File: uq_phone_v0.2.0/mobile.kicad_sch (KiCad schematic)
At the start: 31 parts, among them J3 20279-001E-03, J4 20279-001E-03, Q1 MMBT3904LP-7, Q2 MMBT3904LP-7, U4 WP SNAP-IN BASE_6000636

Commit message: Clean repo
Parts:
- removed R14, R15, R16: 0R, Resistor_SMD:R_0603_1608Metric, symbol Resistors:Resistor_0R
- R12: renamed from R19; footprint Resistor_SMD:R_0603_1608Metric -> Resistor_SMD:R_0402_1005Metric
- R13: renamed from R20; footprint Resistor_SMD:R_0603_1608Metric -> Resistor_SMD:R_0402_1005Metric
- R14: renamed from R21; footprint Resistor_SMD:R_0603_1608Metric -> Resistor_SMD:R_0402_1005Metric
- R15: renamed from R22; footprint Resistor_SMD:R_0603_1608Metric -> Resistor_SMD:R_0402_1005Metric
- renumbered J3 to J4, J4 to J5, R12 to R16, R13 to R18, R18 to R19, TP9 to TP8, TP8 to TP9
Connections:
- net +VMOB renamed VBAT
- net MOB_USB_N: no longer names the net of U4.12 (USB_D-)
- net MOB_USB_P: no longer names the net of U4.13 (USB_D+)
- no-connect marks 39 -> 42

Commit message: Add more footprints, reduce sizes
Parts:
- C10: footprint Capacitor_SMD:C_0402_1005Metric -> Capacitor_SMD:C_0201_0603Metric; LCSC PN C307331 -> C160831
- C11: footprint Capacitor_SMD:C_0402_1005Metric -> Capacitor_SMD:C_0201_0603Metric; LCSC PN C52923 -> C53067
- R12, R13, R14, R15: LCSC PN C95177 -> (none)
- R16, R17: footprint Resistor_SMD:R_0402_1005Metric -> Resistor_SMD:R_0201_0603Metric; LCSC PN C606173 -> C138135
- R18, R19: footprint Resistor_SMD:R_0402_1005Metric -> Resistor_SMD:R_0201_0603Metric; LCSC PN C427250 -> C138139
- TP10, TP11, TP12, TP13, TP14, TP15, TP16, TP8, TP9: footprint TestPoint:TestPoint_Pad_D1.0mm -> TestPoint:TestPoint_Pad_D1.5mm

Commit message: Various Changes to footprints and components
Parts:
- U4: footprint WP_SNAP-IN_BASE:SIERRA_WP_SNAP-IN_BASE -> RC7620_1104625:XCVR_RC7620_1104625
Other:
- note added: "41"
- title: Power System -> UQ Phone

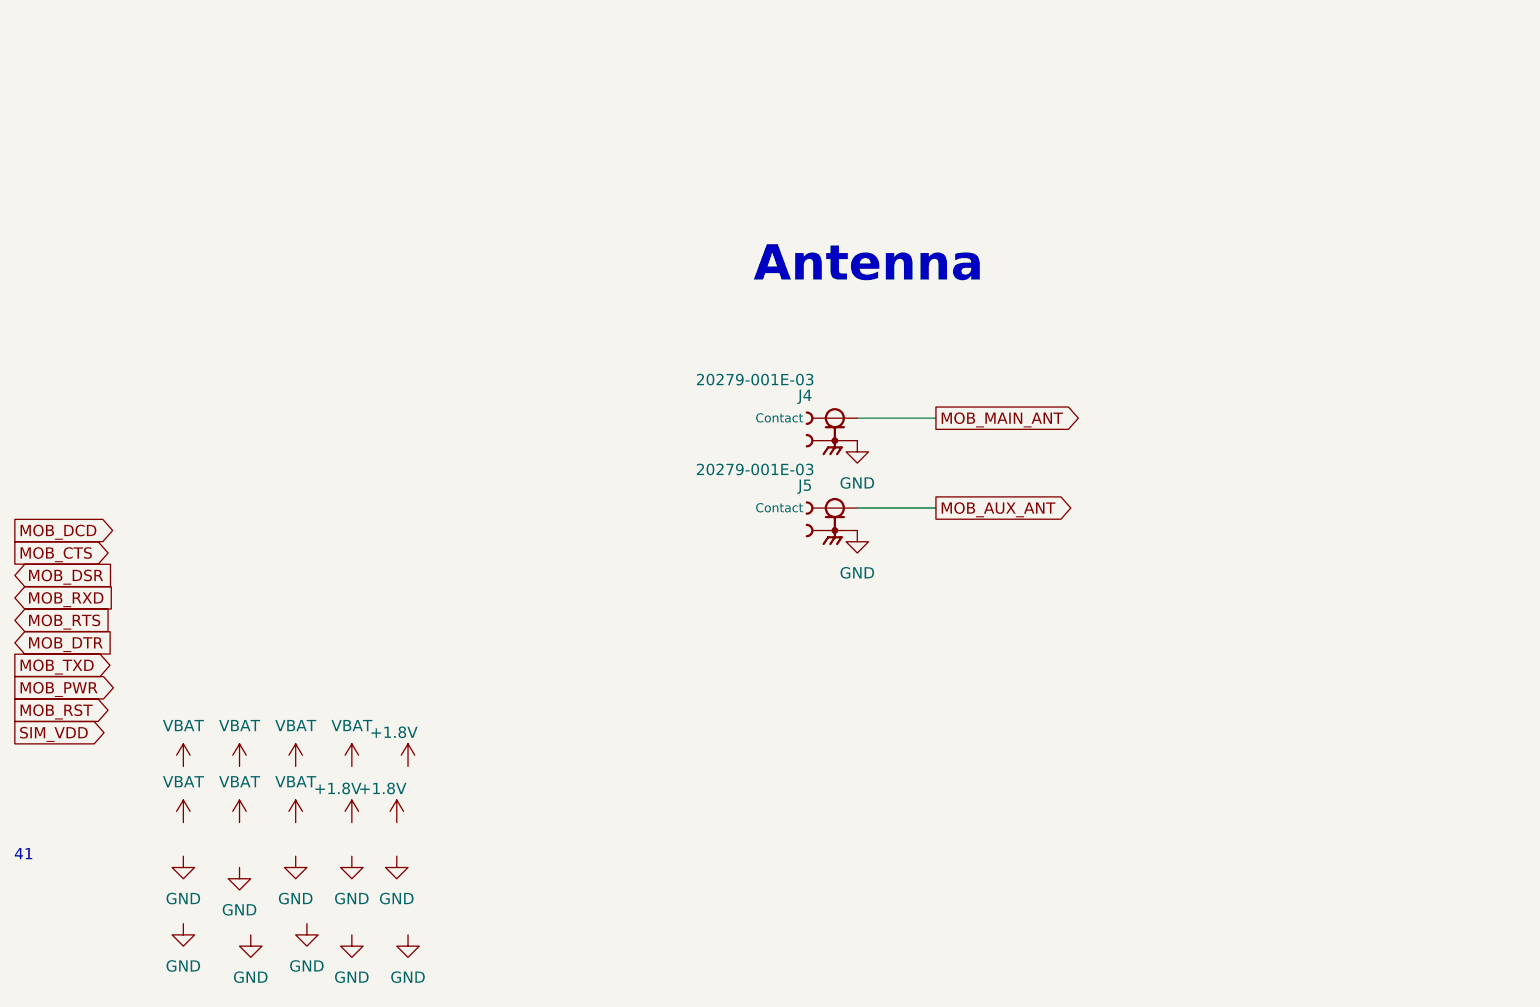
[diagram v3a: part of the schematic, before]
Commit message: Minor Changes - new display
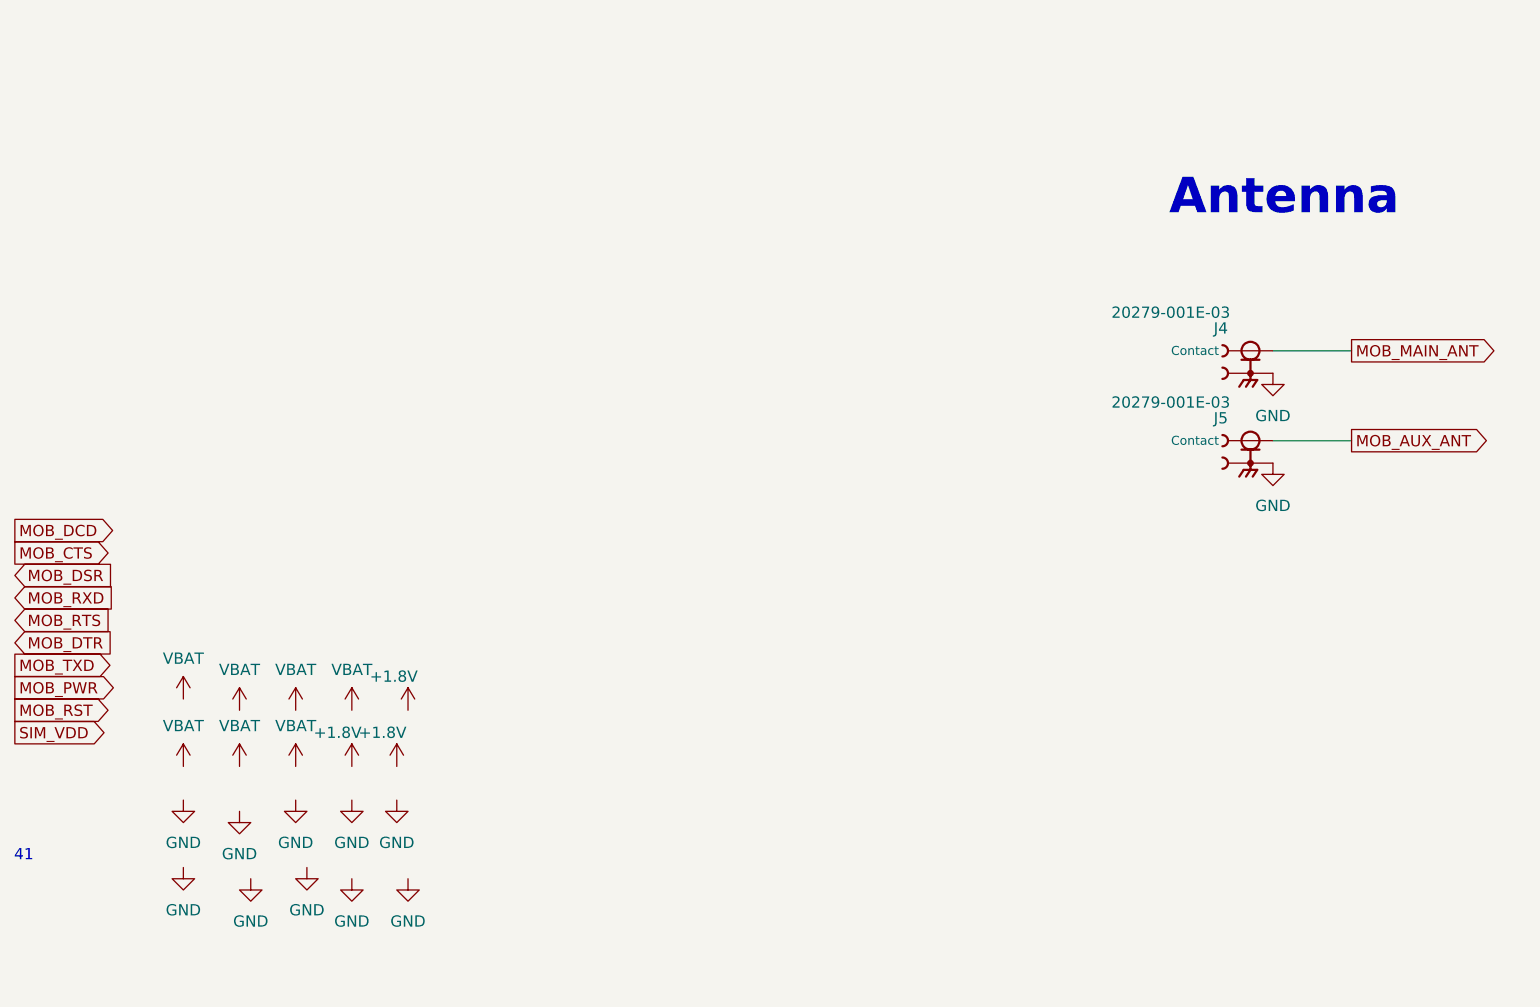
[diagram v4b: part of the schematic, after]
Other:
- moved on the sheet: J4, J5

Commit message: New Layout
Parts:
- removed Q1, Q2: MMBT3904LP-7, MMBT3904LP-7:DFN101X61X53-3N, symbol MMBT3904LP-7:MMBT3904LP-7
- removed R16, R17: 4.7k, Resistor_SMD:R_0201_0603Metric, symbol Resistors:Resistor_4k7
- removed R18, R19: 47k, Resistor_SMD:R_0201_0603Metric, symbol Resistors:Resistor_47k
- added J10, J11: 513382474, 513382474:CON_513382474, symbol 513382474:513382474
- added TP17: TestPoint, TestPoint:TestPoint_Pad_D1.5mm, symbol Connector:TestPoint
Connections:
- net +1.8V: now also J11.10, J11.11, J11.12, J11.9
- net GND: now also J10.23, J10.24, J10.P1, J10.P2, J10.P3, J10.P4, J11.13, J11.14, J11.15, J11.16, J11.17, J11.18, J11.19, J11.20, J11.21, J11.22, J11.23, J11.24, J11.P1, J11.P2, J11.P3, J11.P4
- net SIM_CLK: now also U4.27 (UIM1_CLK); no longer U4.28 (UIM1_DATA)
- net SIM_DATA: now also U4.28 (UIM1_DATA); no longer U4.27 (UIM1_CLK)
- net VBAT: now also J11.1, J11.2, J11.3, J11.4, J11.5, J11.6, J11.7, J11.8, TP17.1
- net MOB_SAFE_PWR_REMOVE: now reaches U4.152 (SAFE_PWR_REMOVE)
- no-connect marks 42 -> 41
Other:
- note added: "0.3A/contact"
- note removed: "41"

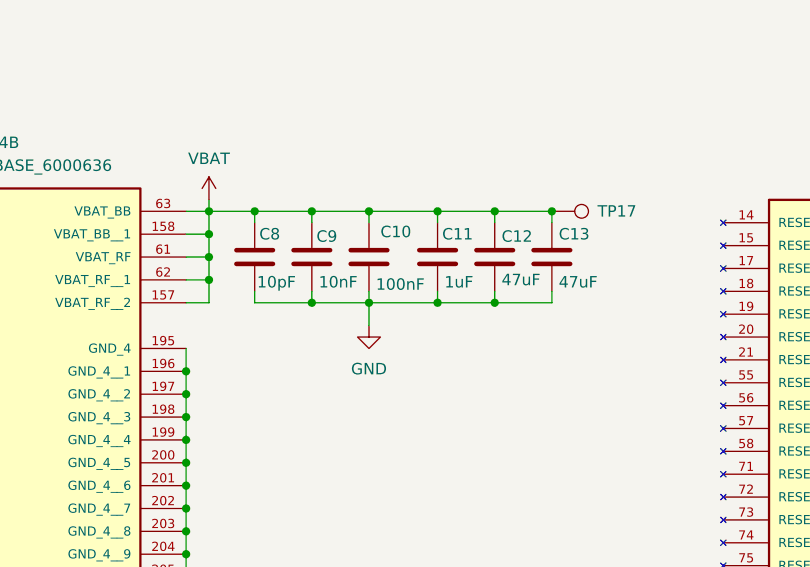
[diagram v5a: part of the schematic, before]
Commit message: Update layout and BL control
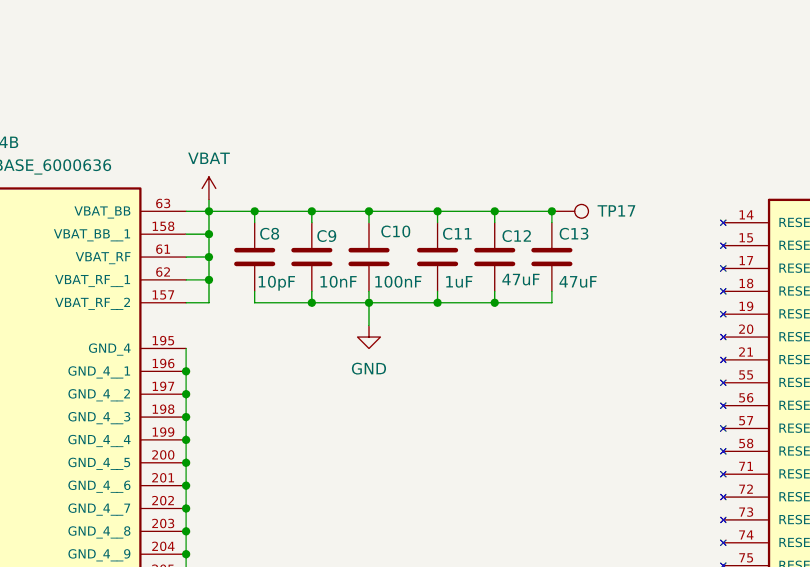
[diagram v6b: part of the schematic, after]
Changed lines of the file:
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@@
 		)
 		(property "Value" "100nF"
-			(at 271.272 46.228 0)
+			(at 271.018 45.974 0)
 			(effects
 				(font

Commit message: Several Hours of Routing
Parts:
- U4: footprint RC7620_1104625:XCVR_RC7620_1104625 -> WP_SNAP-IN_BASE:SIERRA_WP_SNAP-IN_BASE
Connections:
- net +1.8V: now also J11.20, J11.21, J11.22, J11.23; no longer J11.10, J11.11, J11.12, J11.9
- net GND: now also J11.1, J11.10, J11.11, J11.12, J11.2, J11.3, J11.4, J11.5, J11.6, J11.7, J11.8, J11.9; no longer J11.13, J11.14, J11.15, J11.16, J11.17, J11.18, J11.19, J11.20, J11.21, J11.22, J11.23, U4.P1, U4.P10, U4.P11, U4.P12, U4.P13, U4.P14, U4.P15, U4.P16, U4.P17, U4.P18, U4.P19, U4.P2, U4.P20, U4.P3, U4.P4, U4.P5, U4.P6, U4.P7, U4.P8, U4.P9
- net VBAT: now also J11.13, J11.14, J11.15, J11.16, J11.17, J11.18, J11.19; no longer J11.1, J11.2, J11.3, J11.4, J11.5, J11.6, J11.7, J11.8
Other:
- note added: "ADD MORE CAPS"

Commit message: More routing and placements
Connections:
- net MOB_SAFE_PWR_REMOVE is gone; now on net MOB_SAFE_PWR_REMOVE_L: U4.152 (SAFE_PWR_REMOVE)
- net GND: no longer J10.23, J10.24
- net MOB_AUD_BCLK: now also J10.9
- net MOB_AUD_IN: now also J10.10
- net MOB_AUD_OUT: now also J10.11
- net MOB_AUD_SYNC: now also J10.12
- net MOB_CTS: now also J10.18
- net MOB_DCD: now also J10.13
- net MOB_DSR: now also J10.15
- net MOB_DTR: now also J10.14
- net MOB_PWR: now also J10.1
- net MOB_RI: now also J10.20
- net MOB_RST: now also J10.2
- net MOB_RTS: now also J10.17
- net MOB_RXD: now also J10.19
- net MOB_TXD: now also J10.16
- net MOB_WAKE_L: now also J10.4
- net SIM_CLK: now also J10.22
- net SIM_DATA: now also J10.23
- net SIM_RST: now also J10.21
- net SIM_VDD: now also J10.24
- net MOB_SAFE_PWR_REMOVE_L: now reaches J10.3
- net MOB_SYS_CLK: no longer names the net of U4.22 (SYS_CLK)
- no-connect marks 41 -> 42
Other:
- note removed: "50 OHM impedance trace and short as possible"
